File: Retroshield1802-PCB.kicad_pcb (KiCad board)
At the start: 2 copper layers, 99.7 x 53.3 mm, 27 parts, among them J1 Conn_01x17, J10 Conn_01x17, J11 Conn_01x17, J12 Conn_01x17, J2 Conn_01x17, J3 Conn_01x17, J4 Conn_01x17, J5 Conn_01x17, J6 Conn_01x17, J7 Conn_01x17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

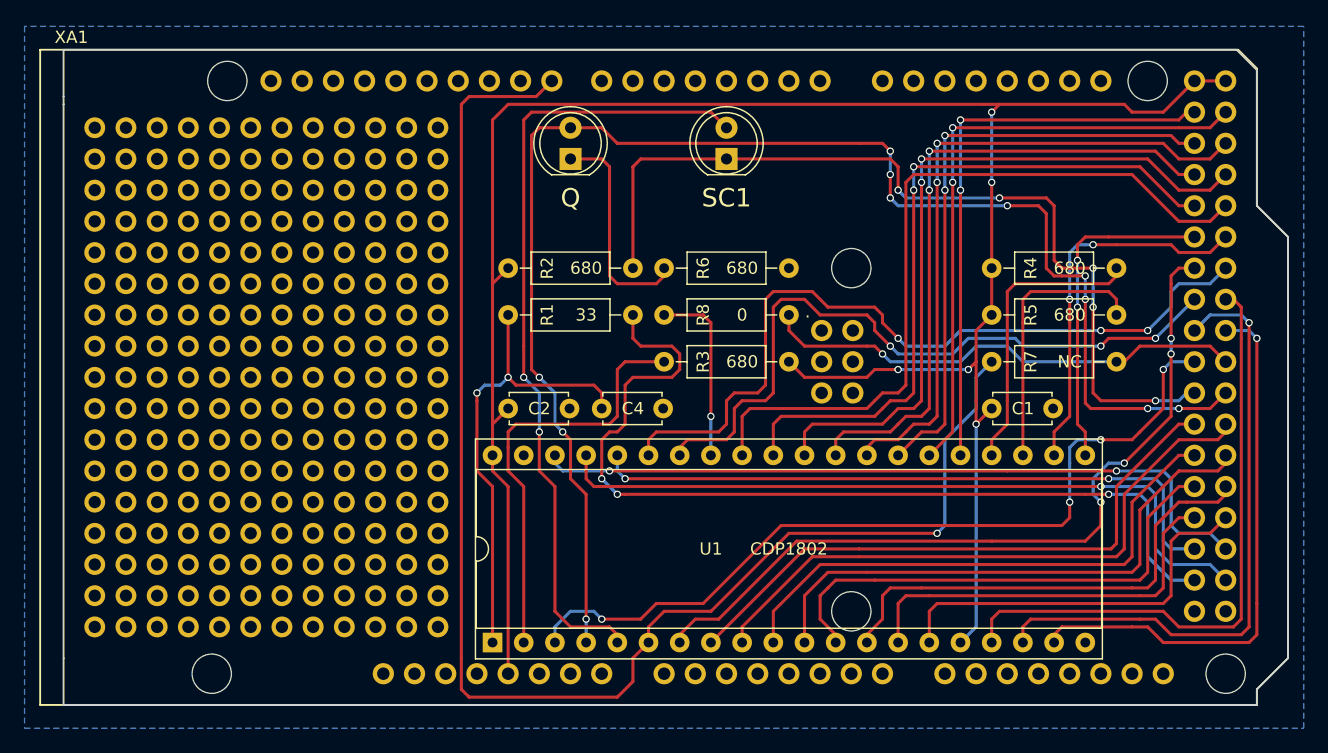
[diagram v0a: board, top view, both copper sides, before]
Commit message: Added header for 0.96" I2C displau
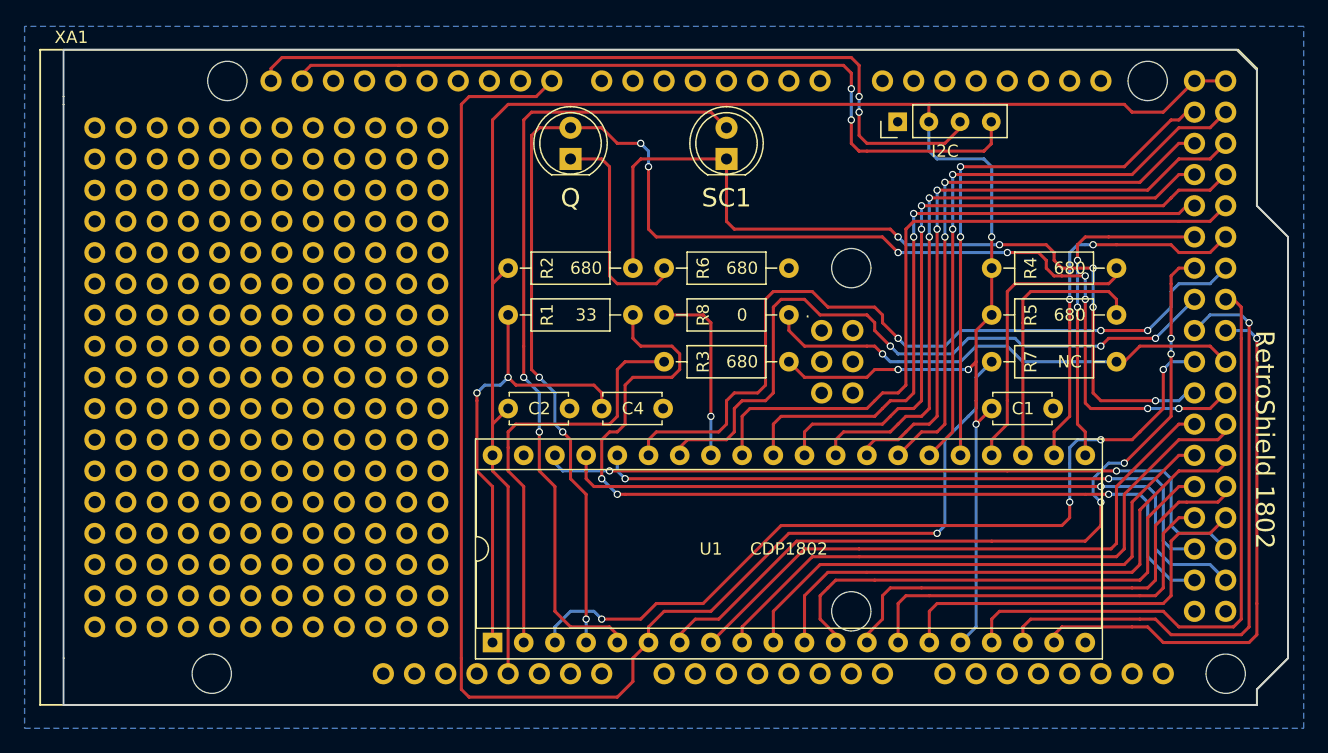
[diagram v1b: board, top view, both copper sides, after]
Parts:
- added IC1: 0.96_I2C_OLED, OLED:0.96_I2C_OLED, F.Cu at (221.6, 53.3)
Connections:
- XA1 pad SCL: (no net) -> Net-(IC1-Pad3)
- XA1 pad SDA: (no net) -> Net-(IC1-Pad4)
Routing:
- net Net-(IC1-Pad4): track 0.00 -> 65.2 mm, vias 0 -> 2
- net Net-(IC1-Pad3): track 0.00 -> 64.8 mm, vias 0 -> 2
- net /MA7: track 62.5 -> 57.1 mm
- net /MA6: track 57.6 -> 52.8 mm
- net /MA5: track 58.5 -> 54.2 mm
- net VCC: track 174.6 -> 178.7 mm, vias 5 -> 4
- net /MA4: track 53.3 -> 49.5 mm
- net /MA3: track 54.2 -> 50.9 mm
- net /MA2: track 48.9 -> 46.2 mm
- net /MA1: track 50.8 -> 48.6 mm
- net /MA0: track 47.3 -> 45.0 mm
- net Q: track 120.8 -> 120.0 mm
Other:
- board text added: "I2C"
- board text added: "RetroShield 1802"

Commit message: Gerber export
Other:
- board text added: "Software and schematic by Erturk Kocalar https://gitlab.com/8bitforce/retroshield1802"
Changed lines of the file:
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@@
     (area 150.419999 50.089999 250.265001 103.580001)
     (thickness 1.6)
-    (drawings 17)
+    (drawings 18)
     (tracks 678)
     (zones 0)
@@
     (visible_elements 7FFFFFFF)
     (pcbplotparams
-      (layerselection 0x00030_80000001)
-      (usegerberextensions false)
+      (layerselection 0x011f0_80000001)
+      (usegerberextensions true)
       (excludeedgelayer true)
       (linewidth 0.100000)
@@
     )
   )
+  (gr_text "Software and schematic by Erturk Kocalar\nhttps://gitlab.com/8bitforce/retroshield1802" (at 210.82 90.805) (layer B.SilkS)
+    (effects (font (size 1 1) (thickness 0.15)) (justify mirror))
+  )
   (gr_text "RetroShield 1802" (at 248.285 81.915 270) (layer F.SilkS)
